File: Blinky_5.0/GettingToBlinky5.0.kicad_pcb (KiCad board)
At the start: 2 copper layers, 7 parts

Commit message: PCB Edited
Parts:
- BT1: moved to B.Cu
- moved R2 21.0 mm to (153.0, 104.0), turned to -90 degrees
- moved R1 20.9 mm to (153.0, 100.0), turned to -90 degrees
- moved BT1 18.9 mm to (146.0, 101.4), turned to 180 degrees
- moved R3 7.88 mm to (140.0, 105.0), turned to -90 degrees
- moved U-2 7.75 mm to (146.0, 102.0)
- moved D1 6.55 mm to (144.0, 107.0), turned to 180 degrees
- moved C1 6.22 mm to (140.0, 101.0), turned to 90 degrees
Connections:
- net Net-(BT1-+) renamed /Vdd
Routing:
- net Net-(U-2-THR): track 0.00 -> 14.7 mm
- net /Vdd: track 0.00 -> 8.56 mm, vias 0 -> 1
- net GND: track 0.00 -> 7.97 mm, vias 0 -> 3
- net Net-(U-2-DIS): track 0.00 -> 6.79 mm
- net (no net): track 0.00 -> 4.22 mm, vias 0 -> 1
- net Net-(U-2-OUT): track 0.00 -> 4.03 mm
- net Net-(D1-A): track 0.00 -> 3.51 mm
- added copper zone on F.Cu, net /Vdd
- added copper zone on B.Cu, net GND
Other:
- board outline added: 32 x 30 mm

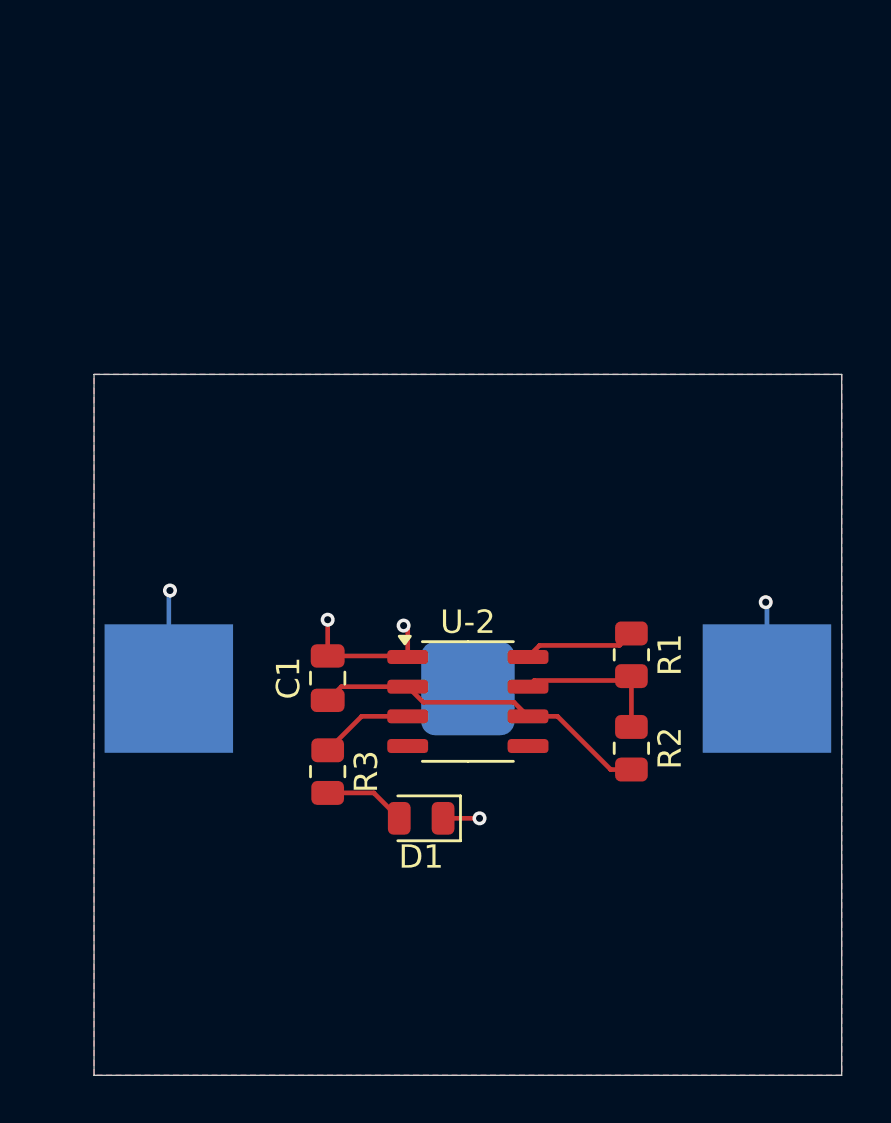
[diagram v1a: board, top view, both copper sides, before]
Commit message: fixed error with footprint of 7555
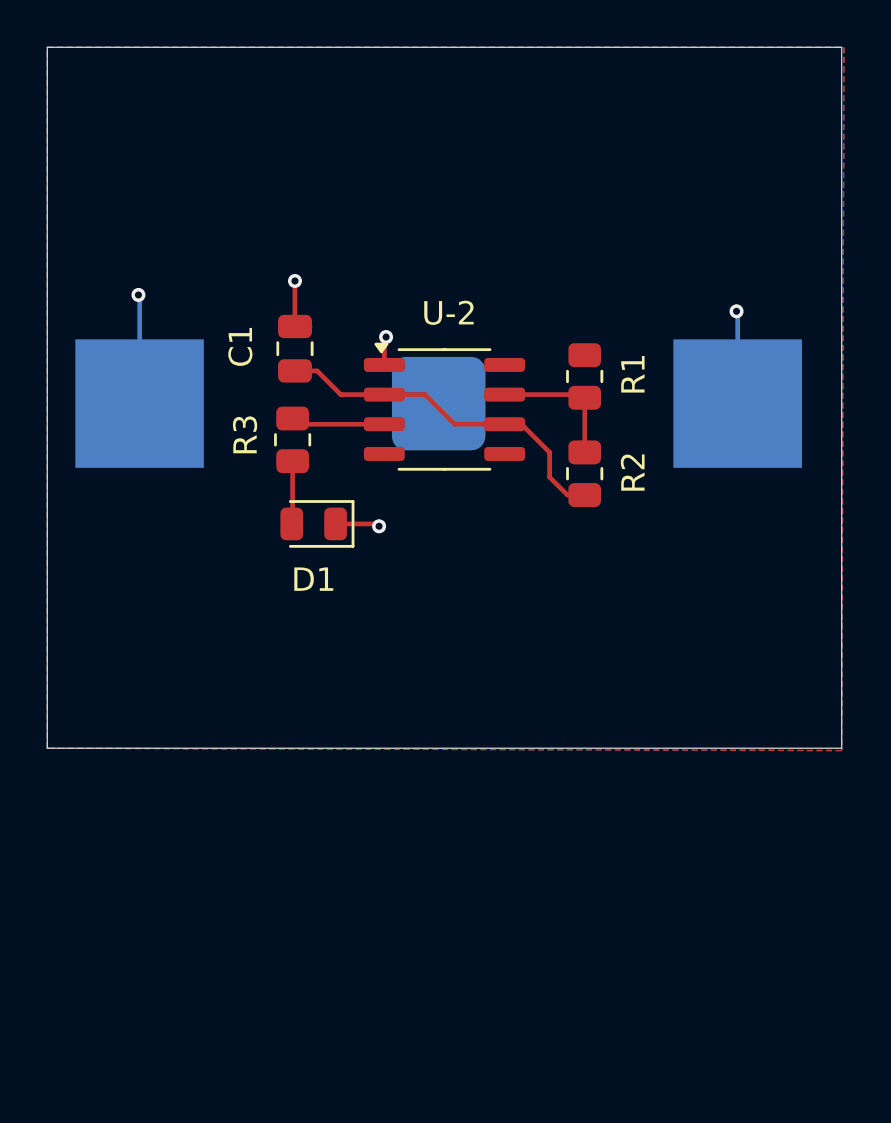
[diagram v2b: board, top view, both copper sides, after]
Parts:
- moved R3 14.3 mm to (138.5, 90.8)
- moved C1 14.2 mm to (138.6, 86.9)
- moved D1 13.4 mm to (139.4, 94.4)
- moved U-2 12.5 mm to (145.0, 89.5)
- moved BT1 12.3 mm to (144.8, 89.2)
- moved R1 12.1 mm to (151.0, 88.1)
- moved R2 11.9 mm to (151.0, 92.2)
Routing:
- net (no net): track 4.22 -> 0.00 mm, vias 1 -> 0
- net GND: track 7.97 -> 5.73 mm
- net Net-(U-2-DIS): track 6.79 -> 5.82 mm
- net Net-(D1-A): track 3.51 -> 2.70 mm
- net Net-(U-2-THR): track 14.7 -> 15.2 mm
- net /Vdd: track 8.56 -> 8.64 mm, vias 1 -> 2
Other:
- board size 32 x 30 mm -> 34 x 30 mm
